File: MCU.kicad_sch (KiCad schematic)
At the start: 6 parts

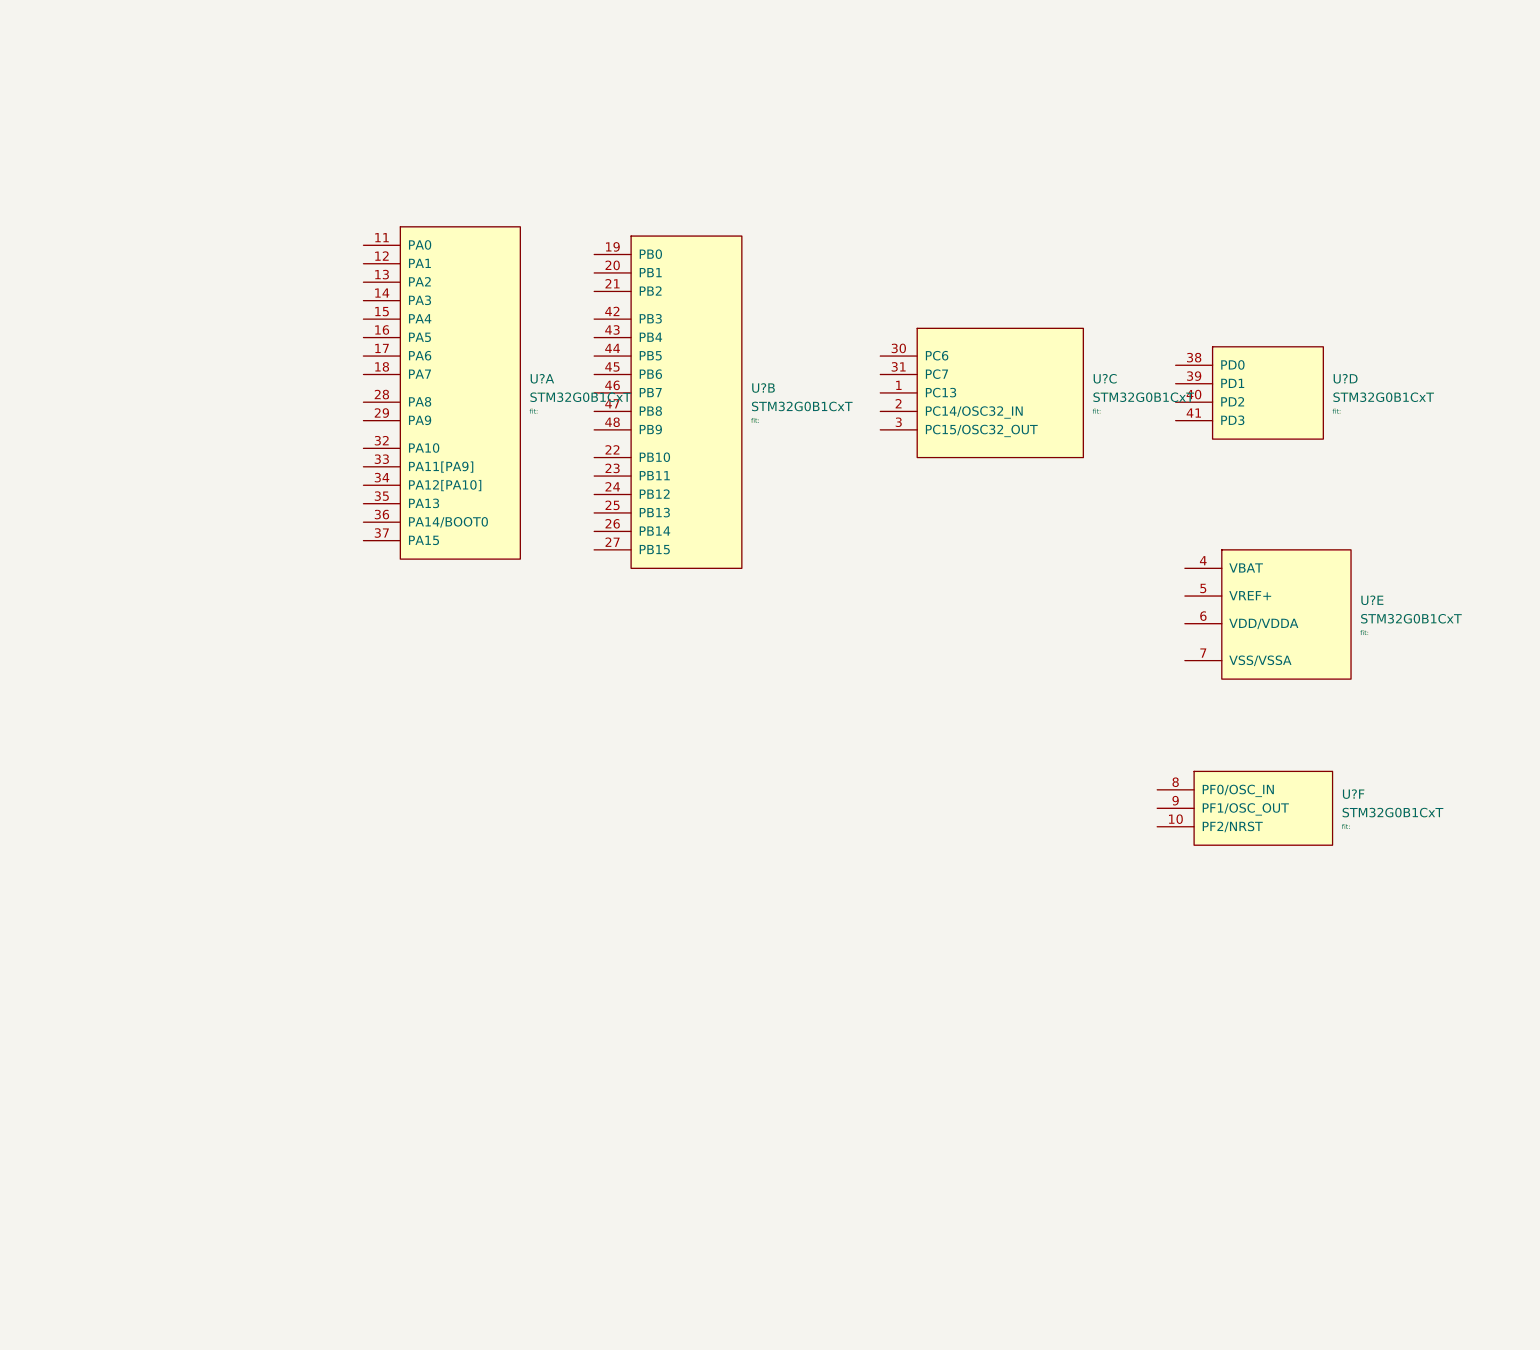
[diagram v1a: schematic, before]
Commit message: Added all parts
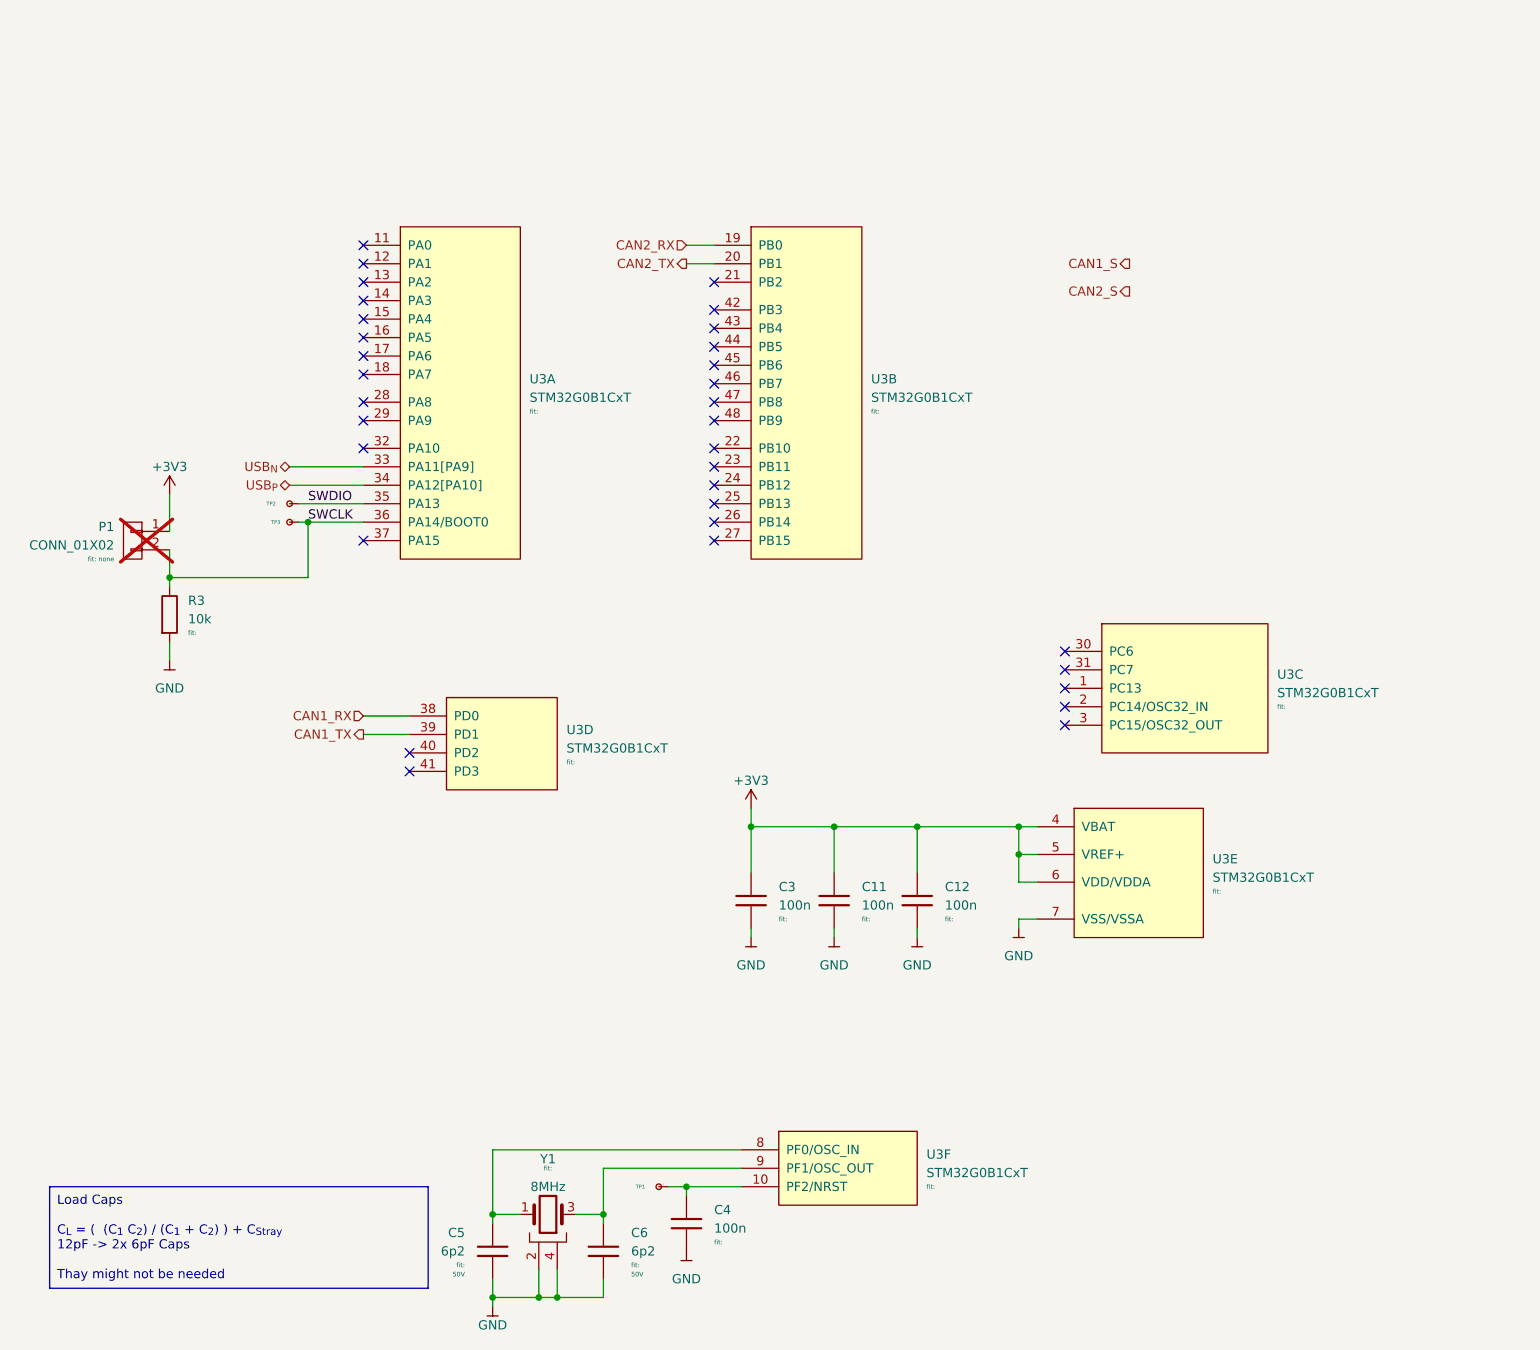
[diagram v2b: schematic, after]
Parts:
- added C11, C12, C3, C4: 100n, Capacitors_SMD:C_0603, symbol multicomp:100n
- added C5, C6: 6p2_0603_C0G_5%_50V_-40C..125C_Chip-Capacitor, Capacitors_SMD:C_0603, symbol Cap_5Percent_E24_0603_C0G_50V_-40C-125C:6p2_0603_C0G_5%_50V_-40C..125C_Chip-Cap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
- added P1: CONN_01X02, Connector_generic:Header_1x2_Pitch2.54mm, symbol generic-connectors:CONN_01X02
- added R3: 10k_0603_100mW_1%_E24_Chip-Resistor, Resistors_SMD:R_0603, symbol Res_1Percent_E24_0603_100mW_-40C-90C:10k_0603_100mW_1%_E24_Chip-Resistor
- added TP1, TP2, TP3: TP1.0mm, Connector_generic:TP1.0mm, symbol generic-connectors:TP1.0mm
- added Y1: 830055299, crystal:Crystal_4Pin_SMD_3.2mmx2.5mm, symbol wuerth:830108313809
- gave numbers to parts that had none: 1
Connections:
- net CAN2_RX: now reaches U3.19 (PB0)
- net CAN2_TX: now reaches U3.20 (PB1)
- net USB_{N}: now reaches U3.33 (PA11[PA9])
- net USB_{P}: now reaches U3.34 (PA12[PA10])
- net SWDIO: now reaches U3.35 (PA13)
- net SWDIO: now also TP2.1
- net SWCLK: now reaches U3.36 (PA14/BOOT0)
- net SWCLK: now also P1.2 (P2), R3.1, TP3.1
- net at U3.10 (PF2/NRST): now also C4.1, TP1.1
- net at U3.8 (PF0/OSC_IN): now also C5.2, Y1.1 (C_{1})
- net at U3.9 (PF1/OSC_OUT): now also C6.2, Y1.3 (C_{2})
- net CAN1_RX: now reaches U3.38 (PD0)
- net CAN1_TX: now reaches U3.39 (PD1)
- net +3V3: now reaches U3.4 (VBAT)
- net +3V3: now also U3.5 (VREF+), U3.6 (VDD/VDDA), C11.1, C12.1, C3.1, P1.1 (P1)
- net GND: now reaches U3.7 (VSS/VSSA)
- net GND: now also C11.2, C12.2, C3.2, C4.2, C5.1, C6.1, R3.2, Y1.2 (GND), Y1.4 (GND)
- no-connect marks 0 -> 33
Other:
- moved on the sheet: U3B, U3C, U3D, U3E, U3F

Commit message: Placement nearly final
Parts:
- removed TP1, TP2, TP3: TP1.0mm, Connector_generic:TP1.0mm, symbol generic-connectors:TP1.0mm
- added X3: TC2030-NL, Connector_Tag-Connect:TC2030-NL, symbol tag-connect:TC2030-NL
- renumbered C5 to C1, C6 to C2, C4 to C3, C3 to C4, C11 to C5, C12 to C6, P1 to P2, R3 to R6, U3 to U1
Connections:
- net +3V3: now also X3.1 (P1)
- net CAN1_S: now also U1.48 (PB9)
- net CAN2_S: now also U1.12 (PA1)
- net GND: now also X3.3 (P3)
- net SWCLK: now also X3.2 (P2)
- net SWDIO: now also X3.4 (P4)
- net NRST: now reaches C3.1, U1.10 (PF2/NRST)
- net NRST: now also X3.5 (P4)
- net at C2.2, U1.9 (PF1/OSC_OUT): now also Y1.1 (C_{1}); no longer Y1.3 (C_{2})
- net LED_RX: now reaches U1.14 (PA3)
- net LED_TX: now reaches U1.15 (PA4)
- net at C1.2, U1.8 (PF0/OSC_IN): now also Y1.3 (C_{2}); no longer Y1.1 (C_{1})
- no-connect marks 33 -> 30
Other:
- moved on the sheet: Y1

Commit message: Update kicad lib
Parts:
- removed U1: STM32G0B1CxT, QFP:LQFP-48_7mmx7mm_Pitch0.5mm, symbol ST:STM32G0B1CxT
- added U5: STM32G0B1CBT, QFP:LQFP-48_7mmx7mm_Pitch0.5mm, symbol ST:STM32G0B1CBT
- X3, Y1: State draft -> reviewed
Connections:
- net +3V3: now also U5.4 (VBAT), U5.5 (VREF+), U5.6 (VDD/VDDA)
- net CAN1_RX: now also U5.38 (PD0)
- net CAN1_S: now also U5.48 (PB9)
- net CAN1_TX: now also U5.39 (PD1)
- net CAN2_RX: now also U5.19 (PB0)
- net CAN2_S: now also U5.12 (PA1)
- net CAN2_TX: now also U5.20 (PB1)
- net GND: now also U5.7 (VSS/VSSA)
- net LED_RX: now also U5.14 (PA3)
- net LED_TX: now also U5.15 (PA4)
- net NRST: now also U5.10 (PF2/NRST)
- net SWCLK: now also U5.36 (PA14/BOOT0)
- net SWDIO: now also U5.35 (PA13)
- net USB_{N}: now also U5.33 (PA11[PA9])
- net USB_{P}: now also U5.34 (PA12[PA10])
- net at C2.2, Y1.1 (C_{1}): now also U5.9 (PF1/OSC_OUT)
- net at C1.2, Y1.3 (C_{2}): now also U5.8 (PF0/OSC_IN)

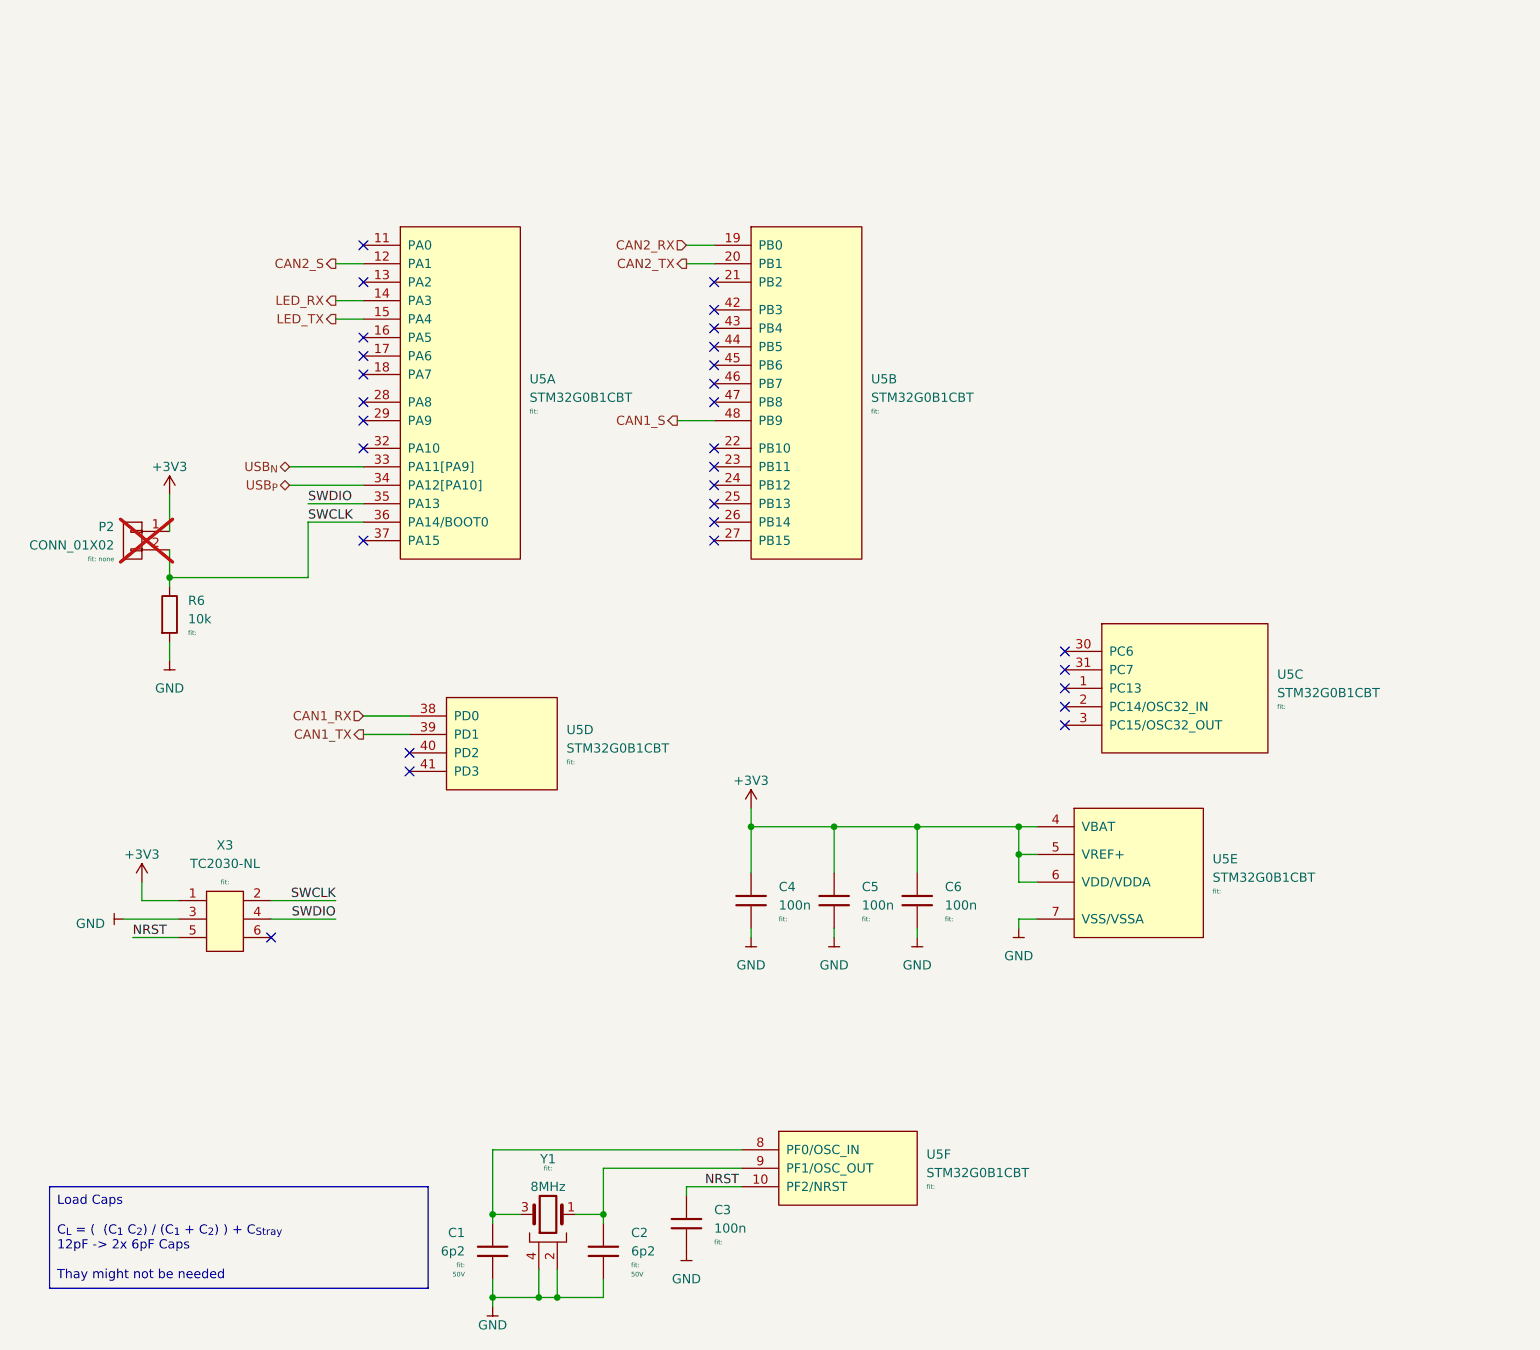
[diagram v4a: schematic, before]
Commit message: Fin rounting
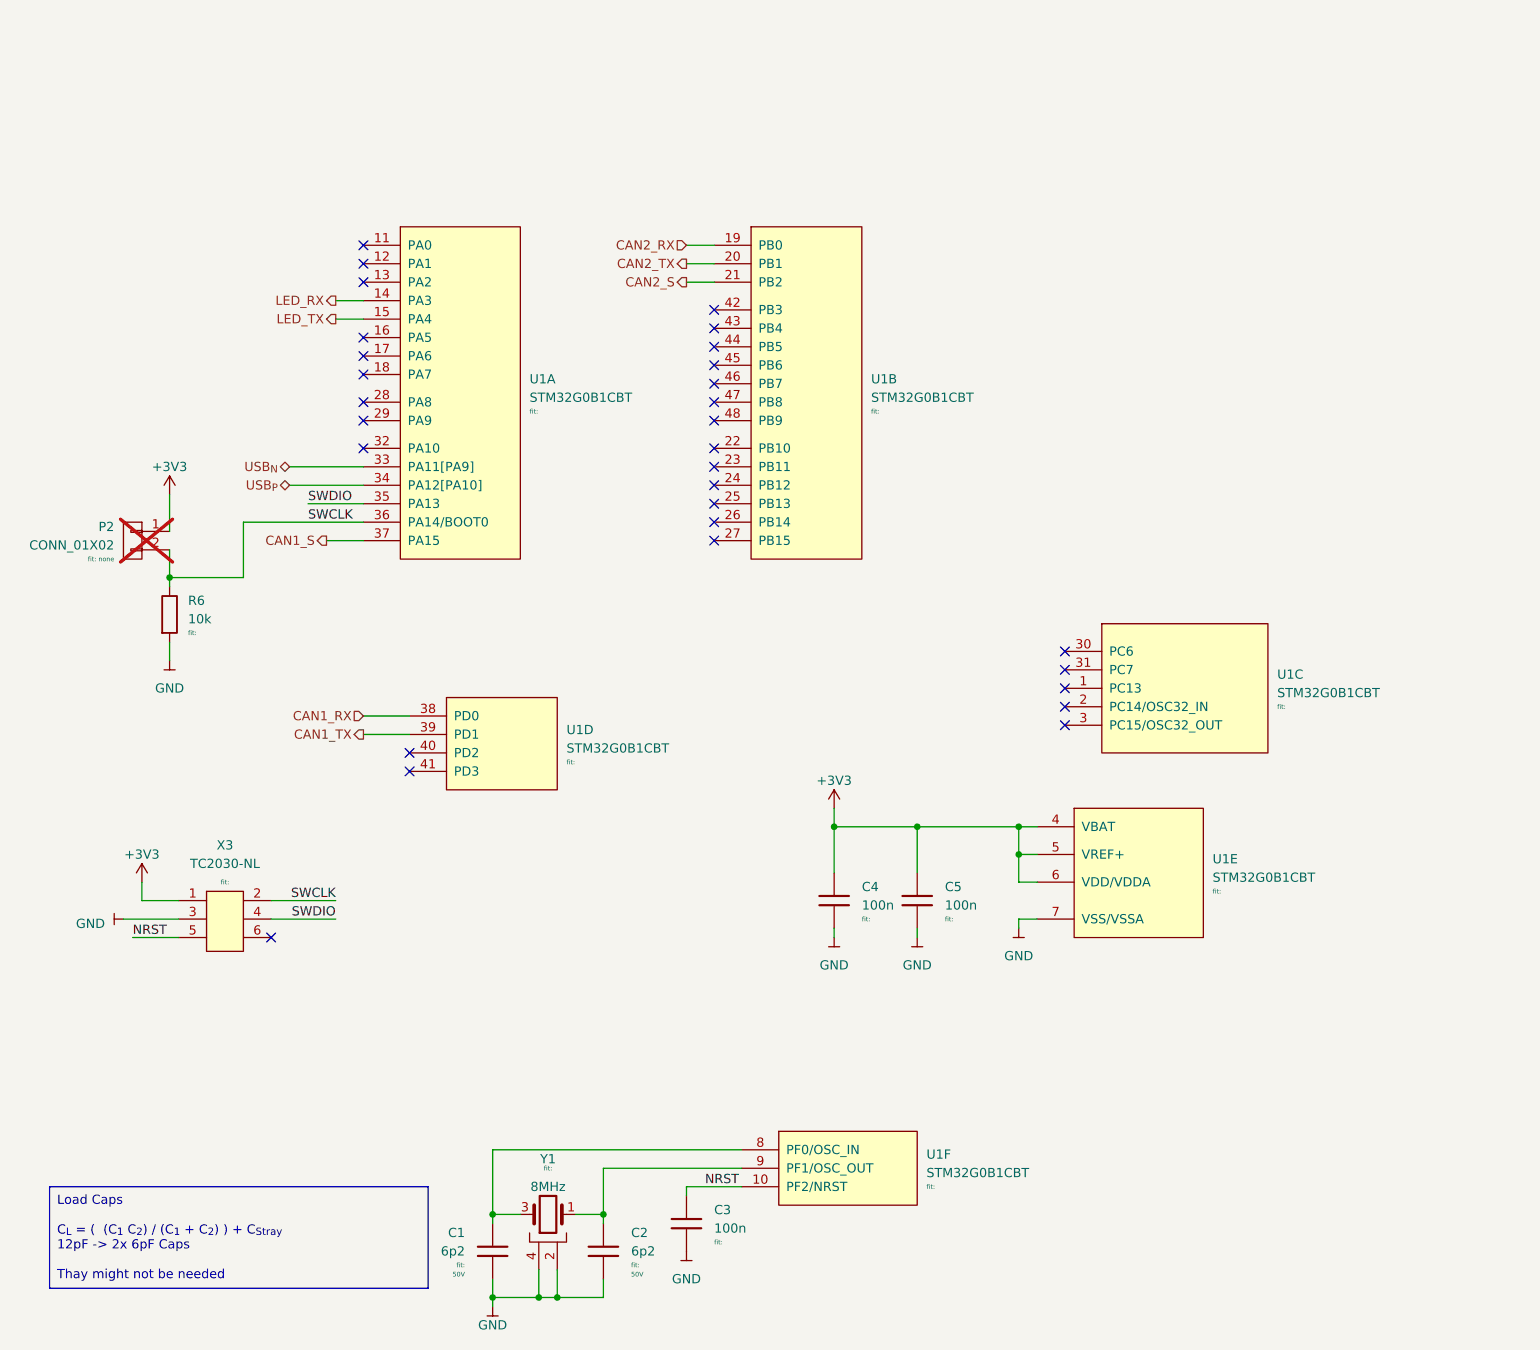
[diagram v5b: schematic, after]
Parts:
- removed C4: 100n, Capacitors_SMD:C_0603, symbol multicomp:100n
- renumbered C5 to C4, C6 to C5, U5 to U1
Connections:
- net CAN1_S: now also U1.37 (PA15); no longer U1.48 (PB9)
- net CAN2_S: now also U1.21 (PB2); no longer U1.12 (PA1)

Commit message: Save after recover
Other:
- moved on the sheet: C1, C2, C3, C4, C5, P2, R6, U1A, U1B, U1C, U1D, U1E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

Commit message: Changes during review
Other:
- company: (none) -> ${company}
- title: (none) -> MCU
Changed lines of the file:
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@@
 (kicad_sch (version 20230121) (generator eeschema)
   (paper "A4")
+  (title_block
+    (title "MCU")
+    (date "2023-06-16")
+    (rev "R${release}")
+    (company "${company}")
+    (comment 1 "${release_state}")
+    (comment 2 "${prefix}-S${type_number}-R${release}-V${sch_variant}-C${sch_ci}")
+    (comment 3 "hardware/${prefix}-S${type_number}_${short_desciption}")
+  )
   (junction (at 40.64 64.77) (diameter 0) (color 0 0 0 0)
   )
